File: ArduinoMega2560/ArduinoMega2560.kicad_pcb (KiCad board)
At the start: 2 copper layers, 116.7 x 69 mm, 73 parts, among them IC5 LM358D, J12 PINHD_1x6_Male, J2 UJ2-BH-1-TH, Q1 Crystal_16MHz, Q2 Crystal_16MHz, SW1 Push_Button, T2 FDN340P, U1 ATmega2560-16A, U2 ATmega8U2-A, U3 LP2986AILD-3.3/NOPB, Y1 TSX-3225_16.0000MF18X-AC0, Y2 TSX-3225_16.0000MF18X-AC0

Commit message: Annotation problem
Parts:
- added C10: 100nF_0603_16V, PCM_4ms_Capacitor:C_0603, F.Cu at (116.0, 99.0)
- moved SW1 187.7 mm to (54.1, 125.7)
- moved U1 127.7 mm to (116.9, 137.5)
- moved L1 58.4 mm to (193.3, 108.7)
- moved F1 56.4 mm to (185.4, 105.1)
- moved J_ADCL 56.4 mm to (163.9, 131.0)
- moved J_PWR 56.4 mm to (199.5, 66.8)
- moved R1 56.4 mm to (181.5, 83.2)
- moved R3 56.4 mm to (181.5, 85.9)
- moved RN1A 56.4 mm to (181.5, 88.6)
- moved C1 56.4 mm to (172.6, 65.8)
- moved C14 56.4 mm to (172.6, 79.1)
- moved C16 56.4 mm to (172.6, 84.4)
- moved C4 56.4 mm to (172.6, 71.1)
- moved C9 56.4 mm to (176.7, 107.3)
- moved ICSP 56.4 mm to (196.9, 80.1)
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- renumbered ICSP2 to ICSP, J_ADCH1 to J_ADCH, J_ADCL1 to J_ADCL, J_COM1 to J_COM, J_PWM1 to J_PWM, J_PWML1 to J_PWML, J_PWR1 to J_PWR, J_XIOH1 to J_XIOH, J_XIOL1 to J_XIOL, LED_L1 to LED_L, LED_ON1 to LED_ON, RN1A1 to RN1A, RN1B1 to RN1B, RN1C1 to RN1C, RN2A1 to RN2A, RN2D1 to RN2D, RN3C1 to RN3C, RN3D1 to RN3D, RN4A1 to RN4A, RN4B1 to RN4B, RN4C1 to RN4C, RN4D1 to RN4D, RN5A1 to RN5A, RN5B1 to RN5B, RN5C1 to RN5C, LED_RX1 to RX, LED_TX1 to TX, IC5 to U3, UBOOT1 to UBOOT, U3 to UP3
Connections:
- U2 pad 27: unconnected-(U2-UCAP-Pad27) -> Net-(U2-UCAP)

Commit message: Daily update
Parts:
- renumbered ICSP to ICSP2, J_ADCH to J_ADCH1, J_ADCL to J_ADCL1, J_COM to J_COM1, J_PWM to J_PWM1, J_PWML to J_PWML1, J_XIOH to J_XIOH1, J_XIOL to J_XIOL1, LED_L to LED_L1, LED_ON to LED_ON1, J_PWR to PWR1, RN1A to RN1A1, RN1B to RN1B1, RN1C to RN1C1, RN2A to RN2A1, RN2D to RN2D1, RN3C to RN3C1, RN3D to RN3D1, RN4A to RN4A1, RN4B to RN4B1, RN4C to RN4C1, RN4D to RN4D1, RN5A to RN5A1, RN5B to RN5B1, RN5C to RN5C1, RX to RX1, TX to TX1, UBOOT to UBOOT1

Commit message: Update label
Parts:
- renumbered J_ADCH1 to ADCH1, LED_L1 to LED_PB7, LED_ON1 to ON1, RN1A1 to RN11, RN1B1 to RN12, RN1C1 to RN13, RN2A1 to RN21, RN2D1 to RN24, RN3C1 to RN33, RN3D1 to RN34, RN4A1 to RN41, RN4B1 to RN42, RN4C1 to RN43, RN4D1 to RN44, RN5A1 to RN51, RN5B1 to RN52, RN5C1 to RN53
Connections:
- net /AREF renamed AREF
- net /ATmega8U2-MU/RESET2 renamed RESET2
- net GND1 renamed GND_3.3V
- C1 pad 1: /RESET -> RESET1
- C13 pad 1: +3.3V -> +3V3
- C2 pad 1: VCC -> VIN
- Cp1 pad 1: VCC -> VIN
- D1 pad 1: VCC -> VIN
- F1 pad 1: /ATmega8U2-MU/USBVCC -> USBVCC
- ICSP2 pad 5: /RESET -> RESET1
- J12 pad 1: /RESET -> RESET1
- J12 pad 6: /VIN -> VIN
- J_PWML1 pad 1: /RXD0 -> RXD0
- J_PWML1 pad 2: /TXD0 -> TXD0
- RESET_EN1 pad 2: /ATmega8U2-MU/RESET -> RESET1
- RN11 pad 1: /RESET -> RESET1
- RN41 pad 2: /ATmega8U2-MU/PE1 -> TXD0
- RN42 pad 2: /ATmega8U2-MU/PE0 -> RXD0
- RN53 pad 2: VCC -> VIN
- SW1 pad 1: /RESET -> RESET1
- T2 pad 3: /Power/USBVCC -> USBVCC
- U1 pad 2: /RXD0 -> RXD0
- U1 pad 3: /TXD0 -> TXD0
- U1 pad 30: /RESET -> RESET1
- U2 pad 31: /ATmega8U2-MU/USBVCC -> USBVCC
- U3 pad 6: +3.3V -> +3V3
- UP1 pad 3: VCC -> VIN
- UP3 pad 5: +3.3V -> +3V3

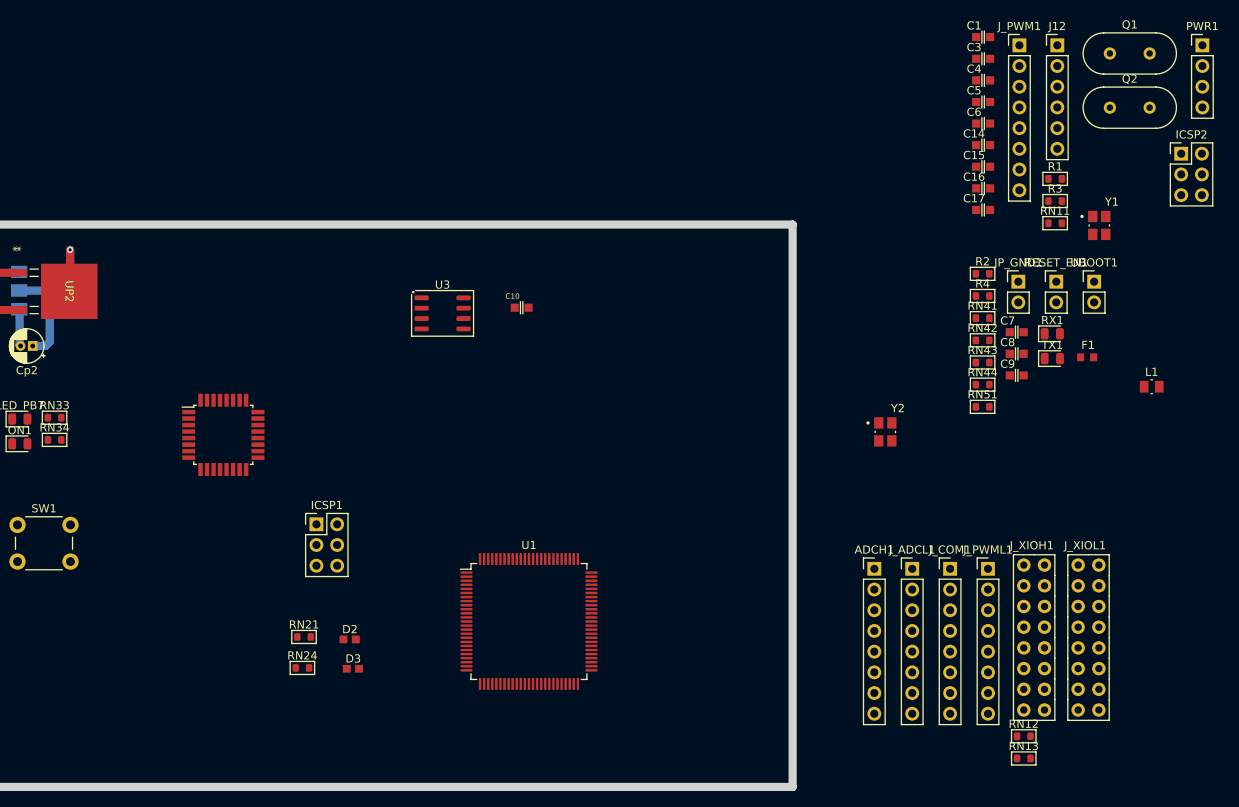
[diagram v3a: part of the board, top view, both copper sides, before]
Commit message: Update label and check dimension size
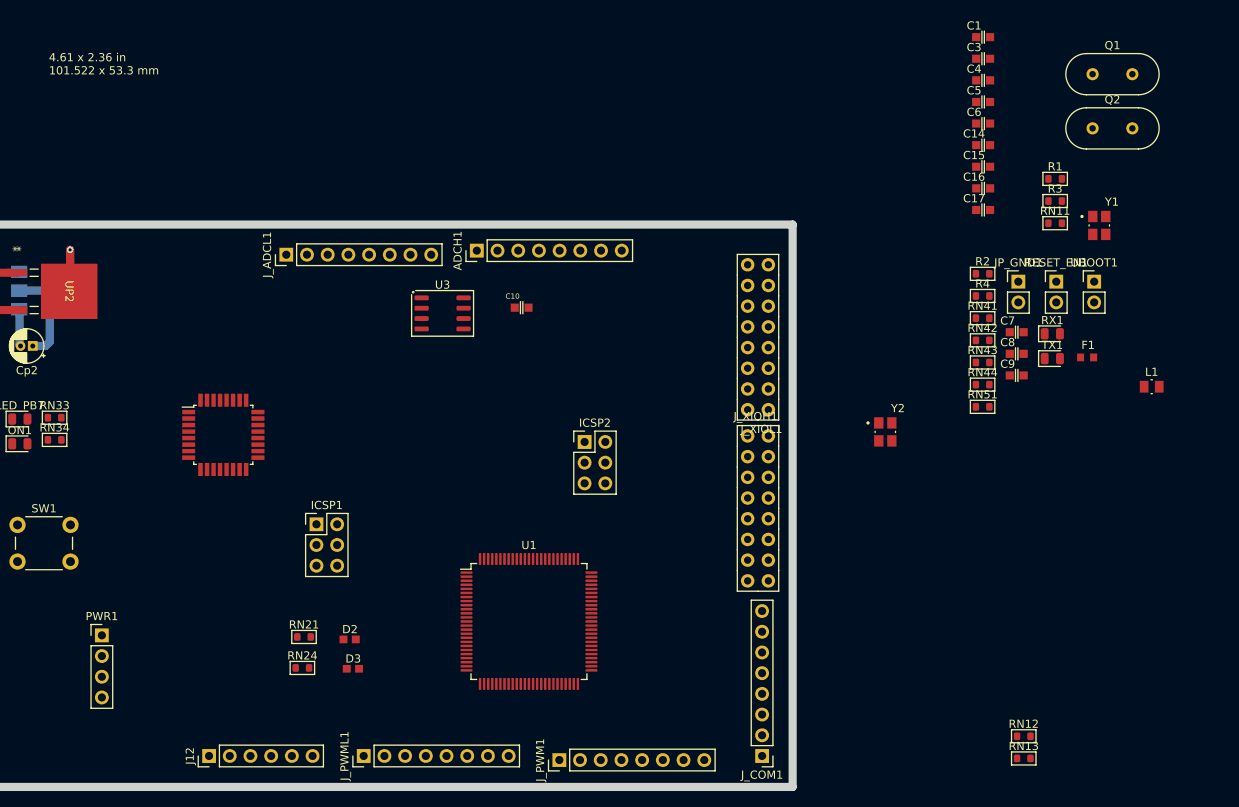
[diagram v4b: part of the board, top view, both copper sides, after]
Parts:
- moved PWR1 153.2 mm to (64.5, 139.2)
- moved J12 135.8 mm to (77.7, 154.0), turned to 90 degrees
- moved J_PWM1 104.3 mm to (120.6, 154.5), turned to 90 degrees
- moved J_ADCL1 85.9 mm to (87.1, 92.5), turned to 90 degrees
- moved ICSP2 81.3 mm to (123.7, 115.5)
- moved J_PWML1 80.0 mm to (96.6, 154.0), turned to 90 degrees
- moved ADCH1 62.5 mm to (110.5, 92.0), turned to 90 degrees
- moved J_XIOL1 54.8 mm to (145.0, 102.6), turned to 180 degrees
- moved J_XIOH1 37.4 mm to (145.0, 123.6)
- moved J_COM1 32.5 mm to (145.5, 154.0), turned to 180 degrees
- moved Q2 3.31 mm to (186.1, 77.0)
- moved Q1 3.31 mm to (186.1, 70.3)
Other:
- board text added: "‎4.61 x 2.36 in 101.522 x 53.3 mm"

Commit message: Confirming the dimension
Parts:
- moved J_PWML1 55.1 mm to (69.3, 106.1)
- moved C2 53.3 mm to (13.4, 145.5)
- moved Cp1 53.3 mm to (17.0, 144.8)
- moved Jack1 53.3 mm to (5.16, 138.0)
- moved UP2 53.3 mm to (27.7, 139.0)
- moved D1 53.3 mm to (14.9, 141.3)
- moved Cp2 53.3 mm to (23.2, 145.7)
- moved UP1 53.3 mm to (24.7, 138.9)
- moved SW1 37.8 mm to (35.8, 92.7)
- moved ICSP1 30.0 mm to (65.2, 110.0)
- moved C15 29.9 mm to (155.3, 106.1)
- moved C17 29.9 mm to (155.3, 111.4)
- moved C3 29.9 mm to (155.3, 92.9)
- moved C5 29.9 mm to (155.3, 98.2)
- moved C6 29.9 mm to (155.3, 100.8)
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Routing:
- net (no net): vias 0 -> 6
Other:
- board text removed: "‎4.61 x 2.36 in 101.522 x 53.3 mm"

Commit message: Tracing
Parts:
- removed the PWR1 at (64.5, 139.2)
- removed UP2: MC33269DTRK-5.0G, ON_Semi-MC33269DTRK-5.0G:DPAK-3_ONS
- added U4: MC33269DTRK-5.0G, LDO_MC33269DTRK-5.0G_Onsemi:DPAK-3_ONS, F.Cu at (63.9, 147.4)
- UP1: moved to F.Cu
- moved L1 117.0 mm to (59.8, 119.2), turned to 180 degrees
- moved F1 111.6 mm to (56.5, 134.6), turned to 180 degrees
- moved D3 47.3 mm to (54.6, 119.2)
- moved D2 46.0 mm to (54.6, 117.4)
- moved U3 44.3 mm to (59.2, 126.0)
- moved Jack1 44.2 mm to (47.6, 150.5)
- moved RN21 43.6 mm to (53.9, 114.0), turned to 90 degrees
- moved RN24 43.4 mm to (57.0, 114.0), turned to -90 degrees
- moved Cp1 39.1 mm to (56.0, 147.2)
- moved C2 37.3 mm to (50.6, 144.5), turned to 180 degrees
- moved Cp2 33.0 mm to (56.0, 142.0), turned to -90 degrees
- moved D1 32.0 mm to (46.9, 141.4)
- moved LED_PB7 27.6 mm to (76.5, 129.3)
- moved C13 26.8 mm to (64.9, 130.0)
- moved RN33 25.8 mm to (80.1, 127.0)
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- renumbered J12 to PWR1
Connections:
- C13 pad 2: GND_3.3V -> GND
- C2 pad 2: GNDPWR -> GND
- Cp1 pad 2: GNDPWR -> GND
- Jack1 pad 2: GNDPWR -> GND
- Jack1 pad 3: GNDPWR -> GND
- RN34 pad 2: /Power/PB7 -> /PB7
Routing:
- net GND: track 4.61 -> 168.6 mm, vias 0 -> 4
- net VIN: track 0.00 -> 98.7 mm, vias 0 -> 2
- net +5V: track 24.9 -> 105.6 mm, vias 1 -> 0
- net +3V3: track 0.00 -> 47.8 mm, vias 0 -> 1
- net GNDPWR: track 45.1 -> 0.00 mm
- net Net-(D2-Pad2): track 0.00 -> 31.9 mm, vias 0 -> 2
- net Net-(JP_GND1-A): track 0.00 -> 24.4 mm, vias 0 -> 1
- net VCC: track 20.2 -> 0.00 mm, vias 2 -> 0
- net Net-(C8-Pad1): track 0.00 -> 18.6 mm, vias 0 -> 1
- net Net-(D3-Pad1): track 0.00 -> 14.6 mm
- net Net-(D2-Pad1): track 0.00 -> 9.71 mm
- net Net-(U3B-+): track 0.00 -> 9.04 mm, vias 0 -> 1
- net /Power/GATE_CMD: track 0.00 -> 8.02 mm
- net Net-(D1-A): track 7.78 -> 14.4 mm
- net RESET1: track 0.00 -> 6.50 mm
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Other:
- board size 116.7 x 69 mm -> 101.6 x 53.3 mm

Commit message: Update Trace
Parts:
- UP2: renamed from U4; footprint LDO_MC33269DTRK-5.0G_Onsemi:DPAK-3_ONS -> LDO_MC33269DTRK_5_0G_Onsemi:DPAK-3_ONS
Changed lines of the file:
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@@
 		(embedded_fonts no)
 	)
-	(footprint "LDO_MC33269DTRK-5.0G_Onsemi:DPAK-3_ONS"
+	(footprint "LDO_MC33269DTRK_5_0G_Onsemi:DPAK-3_ONS"
 		(layer "F.Cu")
 		(at 63.9 147.4045)
 		(tags "MC33269DTRK-5.0G ")
-		(property "Reference" "U4"
+		(property "Reference" "UP2"
 			(at 0 0 0)
 			(unlocked yes)
@@
 		(fp_text user "*"
 			(at -5.215001 6.4135 0)
-			(unlocked yes)
 			(layer "F.SilkS")
 			(effects
@@
 		(fp_text user "*"
 			(at -5.215001 6.4135 0)
+			(unlocked yes)
 			(layer "F.SilkS")
 			(effects
@@
 			"AAAAAAAAAAAAAAAAAAAAAAAAAAAAAAAAAAAAAAAAAAAAAAAAAAAAAAAAAAAAAAAAAAAAAAAAAAAA"
 			"AAAAAAAAAAAAAAAAAAAAAAAAAAAAAAAAAAAAAAAAAAAAAAAAAAAAAAAAAAAAAAAAAAAAAAAAAAAA"
-			"AAA="
+			"AAAAAAAAAAAAAAAAAAAAAAAAAAAAAAAAAAAAAAAAAAAAAAAAAAAAAAAAAAAAAAAAAAAAAAAAAAAA"
+			"AAAAAAAAAAAAAAAAAAAAAAAAAAAAAAAAAAAAAAAAAAAAAAAAAAAAAAAAAAAAAAAAAAAAAAAAAAAA"
+			"AAAAAAAAAAAAAAAAAAAAAAAAAAAAAAAAAAAAAAAAAAAAAAAAAAAAAAAAAAAAAAAAAAAAAAAAAAAA"
+			"AAAAAAAAAAAAAAAAAAAAAAAAAAAAAAAAAAAAAAAAAAAAAAAAAAAAAAAAAAAAAAAAAAAAAAAAAAAA"
+			"AAAAAAAAAAAAAAAAAAAAAAAAAAAAAAAAAAAAAAAAAAAAAAAAAAAAAAAAAAAAAAAAAAAAAAAAAAAA"
+			"AAAAAAAAAAAAAAAAAAAAAAAAAAAAAAAAAAAAAAAAAAAAAAAAAAAAAAAAAAAAAAAAAAAAAAAAAAAA"
+			"AAAAAAAAAAAAAAAAAAAAAAAAAAAAAAAAAAAAAAAAAAAAAAAAAAAAAAAAAAAAAAAAAAAAAAAAAAAA"
+			"AAAAAAAAAAAAAAAAAAAAAAAAAAAAAAAAAAAAAAAAAAAAAAAAAAAAAAAAAAAAAAAAAAAAAAAAAAAA"
+			"AAAAAAAAAAAAAAAAAAAAAAAAAAAAAAAAAAAAAAAAAAAAAAAAAAAAAAAAAAAAAAAAAAAAAAAAAAAA"
+			"AAAAAAAAAAAAAAAAAAAAAAAAAAAAAAAAAAAAAAAAAAAAAAAAAAAAAAAAAAAAAAAAAAAAAAAAAAAA"
+			"AAAAAAAAAAAAAAAAAAAAAAAAAAAAAAAAAAAAAAAAAAAAAAAAAAAAAAAAAAAAAAAAAAAAAAAAAAAA"
+			"AAAAAAAAAAAAAAAAAAAAAAAAAAAAAAAAAAAAAAAAAAAAAAAAAAAAAAAAAAAAAAAAAAAAAAAAAAAA"
+			"AAAAAAAAAAAAAAAAAAAAAAAAAAAAAAAAAAAAAAAAAAAAAAAAAAAAAAAAAAAAAAAAAAAAAAAAAAAA"
+			"AAAAAAAAAAAAAAAAAAAAAAAAAAAAAAAAAAAAAAAAAAAAAAAAAAAAAAAAAAAAAAAAAAAAAAAAAAAA"
+			"AAAAAAAAAAAAAAAAAAAAAAAAAAAAAAAAAAAAAAAAAAAAAAAAAAAAAAAAAAAAAAAAAAAAAAAAAAAA"
+			"AAAAAAAAAAAAAAAAAAAAAAAAAAAAAAAAAAAAAAAAAAAAAAAAAAAAAAAAAAAAAAAAAAAAAAAAAAAA"
+			"AAAAAAAAAAAAAAAAAAAAAAAAAAAAAAAAAAAAAAAAAAAAAAAAAAAAAAAAAAAAAAAAAAAAAAAAAAAA"
+			"AAAAAAAAAAAAAAAAAAAAAAAAAAAAAAAAAAAAAAAAAAAAAAAAAAAAAAAAAAAAAAAAAAAAAAAAAAAA"
+			"AA=="
 		)
 	)
@@
 			"AAAAAAAAAAAAAAAAAAAAAAAAAAAAAAAAAAAAAAAAAAAAAAAAAAAAAAAAAAAAAAAAAAAAAAAAAAAA"
 			"AAAAAAAAAAAAAAAAAAAAAAAAAAAAAAAAAAAAAAAAAAAAAAAAAAAAAAAAAAAAAAAAAAAAAAAAAAAA"
+			"AAAAAAAAAAAAAAAAAAAAAAAAAAAAAAAAAAAAAAAAAAAAAAAAAAAAAAAAAAAAAAAAAAAAAAAAAAAA"
+			"AAAAAAAAAAAAAAAAAAAAAAAAAAAAAAAAAAAAAAAAAAAAAAAAAAAAAAAAAAAAAAAAAAAAAAAAAAAA"
+			"AAAAAAAAAAAAAAAAAAAAAAAAAAAAAAAAAAAAAAAAAAAAAAAAAAAAAAAAAAAAAAAAAAAAAAAAAAAA"
+			"AAAAAAAAAAAAAAAAAAAAAAAAAAAAAAAAAAAAAAAAAAAAAAAAAAAAAAAAAAAAAAAAAAAAAAAAAAAA"
+			"AAAAAAAAAAAAAAAAAAAAAAAAAAAAAAAAAAAAAAAAAAAAAAAAAAAAAAAAAAAAAAAAAAAAAAAAAAAA"
+			"AAAAAAAAAAAAAAAAAAAAAAAAAAAAAAAAAAAAAAAAAAAAAAAAAAAAAAAAAAAAAAAAAAAAAAAAAAAA"
+			"AAAAAAAAAAAAAAAAAAAAAAAAAAAAAAAAAAAAAAAAAAAAAAAAAAAAAAAAAAAAAAAAAAAAAAAAAAAA"
+			"AAAAAAAAAAAAAAAAAAAAAAAAAAAAAAAAAAAAAAAAAAAAAAAAAAAAAAAAAAAAAAAAAAAAAAAAAAAA"
+			"AAAAAAAAAAAAAAAAAAAAAAAAAAAAAAAAAAAAAAAAAAAAAAAAAAAAAAAAAAAAAAAAAAAAAAAAAAAA"
+			"AAAAAAAAAAAAAAAAAAAAAAAAAAAAAAAAAAAAAAAAAAAAAAAAAAAAAAAAAAAAAAAAAAAAAAAAAAAA"
+			"AAAAAAAAAAAAAAAAAAAAAAAAAAAAAAAAAAAAAAAAAAAAAAAAAAAAAAAAAAAAAAAAAAAAAAAAAAAA"
+			"AAAAAAAAAAAAAAAAAAAAAAAAAAAAAAAAAAAAAAAAAAAAAAAAAAAAAAAAAAAAAAAAAAAAAAAAAAAA"
+			"AAAAAAAAAAAAAAAAAAAAAAAAAAAAAAAAAAAAAAAAAAAAAAAAAAAAAAAAAAAAAAAAAAAAAAAAAAAA"
+			"AAAAAAAAAAAAAAAAAAAAAAAAAAAAAAAAAAAAAAAAAAAAAAAAAAAAAAAAAAAAAAAAAAAAAAAAAAAA"
+			"AAAAAAAAAAAAAAAAAAAAAAAAAAAAAAAAAAAAAAAAAAAAAAAAAAAAAAAAAAAAAAAAAAAAAAAAAAAA"
+			"AAAAAAAAAAAAAAAAAAAAAAAAAAAAAAAAAAAAAAAAAAAAAAAAAAAAAAAAAAAAAAAAAAAAAAAAAAAA"
+			"AAAAAAAAAAAAAAAAAAAAAAAAAAAAAAAAAAAAAAAAAAAAAAAAAAAAAAAAAAAAAAAAAAAAAAAAAAAA"
+			"AAAAAAAAAAAAAAAAAAAAAAAAAAAAAAAAAAAAAAAAAAAAAAAAAAAAAAAAAAAAAAAAAAAAAAAAAAAA"

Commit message: Update
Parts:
- moved C8 104.6 mm to (55.2, 119.7)
- moved R2 90.6 mm to (65.7, 133.2), turned to 90 degrees
- moved Y2 88.6 mm to (69.0, 133.2), turned to -90 degrees
- moved R4 85.4 mm to (70.1, 129.6), turned to 90 degrees
- moved LED_PB7 16.9 mm to (62.5, 119.8)
- moved RN34 16.9 mm to (66.1, 119.8)
- moved ON1 16.9 mm to (62.5, 117.5)
- moved RN33 16.9 mm to (66.1, 117.5)
- moved U1 4.80 mm to (97.9, 131.9)
- moved D3 3.13 mm to (55.1, 116.1)
- moved RN21 2.67 mm to (56.5, 113.4)
- moved RN24 2.67 mm to (54.4, 113.4)
- moved U2 1.61 mm to (79.1, 116.3)
- moved L1 1.33 mm to (58.5, 118.9), turned to 90 degrees
- moved C11 0.92 mm to (54.0, 126.2), turned to 90 degrees
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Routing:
- net GND: track 168.6 -> 210.4 mm, vias 4 -> 5
- net +5V: track 105.6 -> 90.1 mm
- net Net-(D2-Pad1): track 9.71 -> 21.9 mm, vias 0 -> 1
- net Net-(D3-Pad1): track 14.6 -> 22.4 mm
- net Net-(R2-Pad2): track 0.00 -> 7.77 mm
- net Net-(JP_GND1-A): track 24.4 -> 18.0 mm
- net Net-(D2-Pad2): track 31.9 -> 37.5 mm, vias 2 -> 1
- net Net-(U2-PC0/XTAL2): track 0.00 -> 2.21 mm
- net Net-(ON1-A): track 0.00 -> 1.84 mm
- net Net-(LED_PB7-A): track 0.00 -> 1.84 mm
- net Net-(C8-Pad1): track 18.6 -> 19.4 mm, vias 1 -> 2
